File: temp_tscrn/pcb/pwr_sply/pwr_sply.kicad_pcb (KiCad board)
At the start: 2 copper layers, 55 x 38 mm, 11 parts, among them J1 Screw_Terminal_01x03, J2 Conn_01x03_Male, Q1 Q_PMOS_GSD, U1 TLV75533PDBV

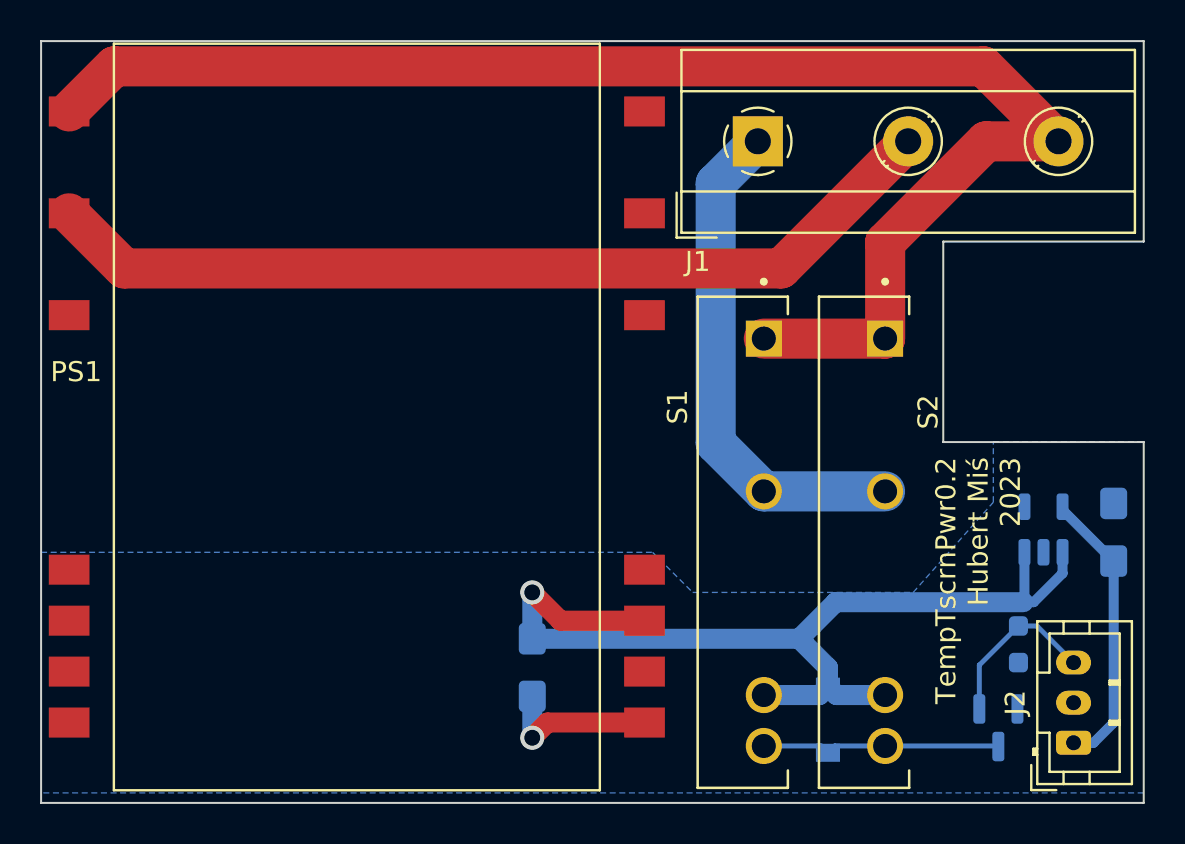
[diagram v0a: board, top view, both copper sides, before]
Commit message: temp_tscrn: pcb v3
Version 3 of power supply for temp_tscrn PCB. This one uses triac and
optotriac to control the heater
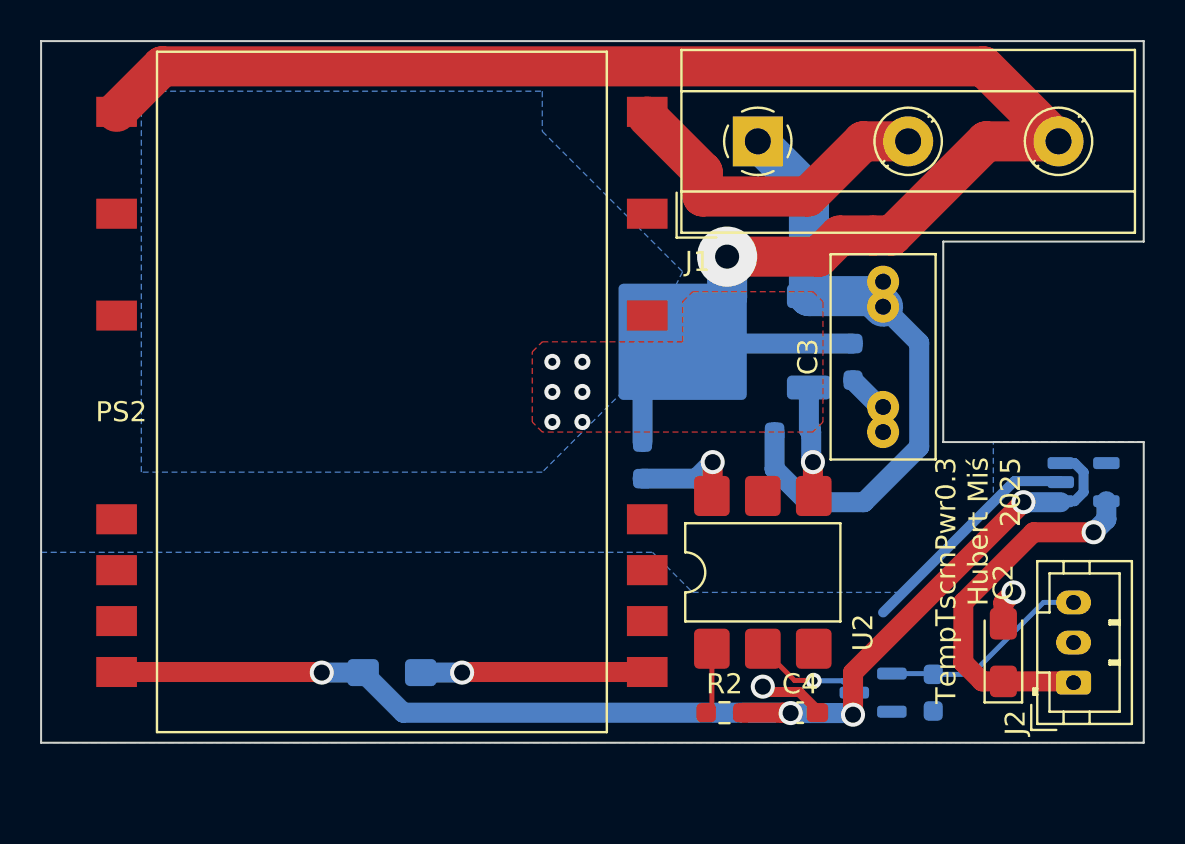
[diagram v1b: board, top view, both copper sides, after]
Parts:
- removed D1: D, Diode_SMD:D_SOD-123
- removed PS1: IRM-03-5S, Converter_ACDC:Converter_ACDC_MeanWell_IRM-03-xx_SMD
- removed S1, S2: AQG22105, pwr_sply:RELAY_AQG22105
- added C3: 0.01u, Capacitor_THT:C_Rect_L10.0mm_W5.0mm_P5.00mm_P7.50mm, F.Cu at (92.0, 89.5)
- added C4: 100n, Capacitor_SMD:C_0603_1608Metric_Pad1.08x0.95mm_HandSolder, F.Cu at (87.9, 103.5)
- added PS2: IRM-02-5S, Converter_ACDC:Converter_ACDC_MeanWell_IRM-02-xx_SMD, F.Cu at (67.0, 87.5)
- added Q2: BT136-600, Package_TO_SOT_SMD:TO-252-2, B.Cu at (83.3, 85.0)
- added R2: 330, Resistor_SMD:R_0603_1608Metric_Pad0.98x0.95mm_HandSolder, F.Cu at (84.1, 103.5)
- added R3: 360, Resistor_SMD:R_0603_1608Metric_Pad0.98x0.95mm_HandSolder, B.Cu at (80.0, 90.9)
- added R4: 360, Resistor_SMD:R_0603_1608Metric_Pad0.98x0.95mm_HandSolder, B.Cu at (87.5, 89.5)
- added R5: 39, Resistor_SMD:R_0603_1608Metric_Pad0.98x0.95mm_HandSolder, B.Cu at (90.5, 86.0)
- added U2: MOC3063S, Package_DIP:SMDIP-6_W7.62mm, F.Cu at (86.0, 96.5)
- C1: value C_Polarized -> 10u
- C2: value C_Polarized -> 10u; moved to F.Cu
- Q1: value Q_PMOS_GSD -> Q_NMOS_GSD
- R1: value R -> 10k
- moved C2 8.14 mm to (98.0, 100.5)
- moved C1 7.00 mm to (67.5, 101.5), turned to 0 degrees
- moved Q1 6.49 mm to (91.5, 102.5), turned to 180 degrees
- moved R1 4.89 mm to (94.5, 102.5)
- moved U1 3.10 mm to (102.0, 92.0), turned to 0 degrees
- moved J2 3.00 mm to (101.5, 102.0)
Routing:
- net NEUT: track 45.6 -> 16.5 mm
- net GND: track 7.98 -> 28.0 mm, vias 1 -> 3
- net LINE: track 73.4 -> 87.9 mm, vias 0 -> 7
- net VCC: track 49.2 -> 59.6 mm, vias 1 -> 4
- net Net-(Q1-D): track 12.0 -> 5.47 mm, vias 0 -> 1
- net /pwr_out: track 25.4 -> 31.3 mm
- net /TOOUT1: track 0.00 -> 5.55 mm, vias 0 -> 1
- net /TOOUT2: track 0.00 -> 5.51 mm, vias 0 -> 1
- net +3.3V: track 14.2 -> 18.7 mm, vias 0 -> 1
- net Net-(R2-Pad1): track 0.00 -> 3.31 mm
- net Net-(C3-Pad1): track 0.00 -> 2.22 mm
- net /pwr_en: track 8.45 -> 10.6 mm
- added copper zone on B.Cu, net LINE
- added copper zone on F.Cu, net LINE
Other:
- board size 55 x 38 mm -> 55 x 35 mm
- board text added: "L"
- board text added: "N"
- board text added: "OUT"
- board text added: "TempTscrnPwr0.3 Hubert Miś 2025"
- board text removed: "TempTscrnPwr0.2 Hubert Miś 2023"
